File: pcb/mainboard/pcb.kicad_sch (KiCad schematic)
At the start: 3 parts, among them U1 ESP32-C6-MINI-1

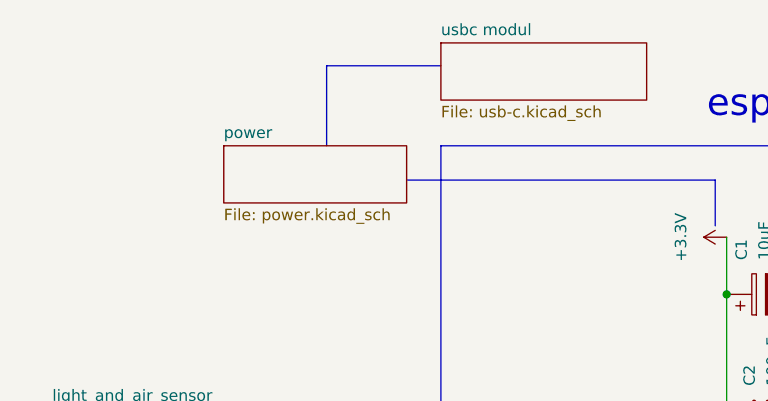
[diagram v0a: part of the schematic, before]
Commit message: making separate pcbs
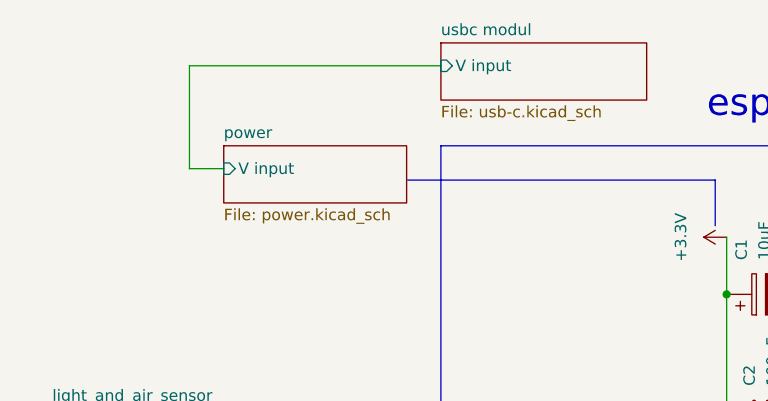
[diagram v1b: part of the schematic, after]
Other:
- sheet power ports: added V input; removed none
- sheet usbc modul ports: added V input; removed none
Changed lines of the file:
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@@
+	(wire
+		(pts
+			(xy 97.79 69.85) (xy 69.85 69.85)
+		)
+		(stroke
+			(width 0)
+			(type default)
+		)
+	)
 	(wire
 		(pts
@@
 		)
 	)
+	(wire
+		(pts
+			(xy 81.28 156.21) (xy 114.3 156.21)
+		)
+		(stroke
+			(width 0)
+			(type default)
+		)
+	)
+	(wire
+		(pts
+			(xy 114.3 147.32) (xy 111.76 147.32)
+		)
+		(stroke
+			(width 0)
+			(type default)
+		)
+	)
+	(wire
+		(pts
+			(xy 187.96 137.16) (xy 190.5 137.16)
+		)
+		(stroke
+			(width 0)
+			(type default)
+		)
+	)
+	(wire
+		(pts
+			(xy 129.54 95.25) (xy 129.54 109.22)
+		)
+		(stroke
+			(width 0)
+			(type default)
+		)
+	)
+	(wire
+		(pts
+			(xy 144.78 152.4) (xy 168.91 152.4)
+		)
+		(stroke
+			(width 0)
+			(type default)
+		)
+	)
+	(wire
+		(pts
+			(xy 69.85 69.85) (xy 69.85 81.28)
+		)
+		(stroke
+			(width 0)
+			(type default)
+		)
+	)
+	(wire
+		(pts
+			(xy 137.16 95.25) (xy 137.16 109.22)
+		)
+		(stroke
+			(width 0)
+			(type default)
+		)
+	)
+	(wire
+		(pts
+			(xy 165.1 121.92) (xy 144.78 121.92)
+		)
+		(stroke
+			(width 0)
+			(type default)
+		)
+	)
+	(wire
+		(pts
+			(xy 114.3 156.21) (xy 114.3 149.86)
+		)
+		(stroke
+			(width 0)
+			(type default)
+		)
+	)
 	(polyline
 		(pts
-			(xy 85.09 78.74) (xy 85.09 69.85)
-		)
-		(stroke
-			(width 0)
-			(type default)
-		)
-	)
-	(wire
-		(pts
-			(xy 81.28 156.21) (xy 114.3 156.21)
-		)
-		(stroke
-			(width 0)
-			(type default)
-		)
-	)
-	(wire
-		(pts
-			(xy 114.3 147.32) (xy 111.76 147.32)
-		)
-		(stroke
-			(width 0)
-			(type default)
-		)
-	)
-	(wire
-		(pts
-			(xy 187.96 137.16) (xy 190.5 137.16)
-		)
-		(stroke
-			(width 0)
-			(type default)
-		)
-	)
-	(wire
-		(pts
-			(xy 129.54 95.25) (xy 129.54 109.22)
-		)
-		(stroke
-			(width 0)
-			(type default)
-		)
-	)
-	(wire
-		(pts
-			(xy 144.78 152.4) (xy 168.91 152.4)
-		)
-		(stroke
-			(width 0)
-			(type default)
-		)
-	)
-	(wire
-		(pts
-			(xy 137.16 95.25) (xy 137.16 109.22)
-		)
-		(stroke
-			(width 0)
-			(type default)
-		)
-	)
-	(wire
-		(pts
-			(xy 165.1 121.92) (xy 144.78 121.92)
-		)
-		(stroke
-			(width 0)
-			(type default)
-		)
-	)
-	(wire
-		(pts
-			(xy 114.3 156.21) (xy 114.3 149.86)
-		)
-		(stroke
-			(width 0)
-			(type default)
-		)
-	)
-	(polyline
-		(pts
 			(xy 53.34 139.7) (xy 50.8 139.7)
 		)
@@
 		)
 	)
-	(polyline
-		(pts
-			(xy 85.09 69.85) (xy 97.79 69.85)
-		)
-		(stroke
-			(width 0)
-			(type default)
-		)
-	)
 	(wire
 		(pts
@@
 		(pts
 			(xy 81.28 137.16) (xy 114.3 137.16)
+		)
+		(stroke
+			(width 0)
+			(type default)
+		)
+	)
+	(wire
+		(pts
+			(xy 69.85 81.28) (xy 73.66 81.28)
 		)
 		(stroke
@@
 			)
 		)
+		(pin "V input" input
+			(at 97.79 69.85 180)
+			(effects
+				(font
+					(size 1.27 1.27)
+				)
+				(justify left)
+			)
+		)
 		(instances
 			(project "pcb"
@@
 			)
 		)
+		(pin "V input" input
+			(at 73.66 81.28 180)
+			(effects
+				(font
+					(size 1.27 1.27)
+				)
+				(justify left)
+			)
+		)

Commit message: fixing bugs in the frimware
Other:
- removed sheet light_and_air_sensor
